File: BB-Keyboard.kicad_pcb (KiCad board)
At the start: 2 copper layers, 41 parts, among them P1 CONN_01X04, SW1 SW_Q, SW10 SW_X, SW11 SW_0, SW12 SW_R, SW13 SW_F, SW14 SW_C, SW15 SW_T, SW16 SW_G, SW17 SW_V, SW18 SW_SPC, SW19 SW_Y, SW2 SW_A, SW20 SW_H, SW21 SW_B, SW22 SW_U, SW23 SW_J, SW24 SW_N, SW25 SW_I, SW26 SW_K, SW27 SW_M, SW28 SW_SYM, SW29 SW_O, SW3 SW_ALT, SW30 SW_L, SW31 SW_$, SW32 SW_RSHIFT, SW33 SW_P, SW34 SW_BK, SW35 SW_ENT, SW4 SW_W, SW5 SW_S, SW6 SW_Z, SW7 SW_LSHIFT, SW8 SW_E, SW9 SW_D, U1 TCA8418

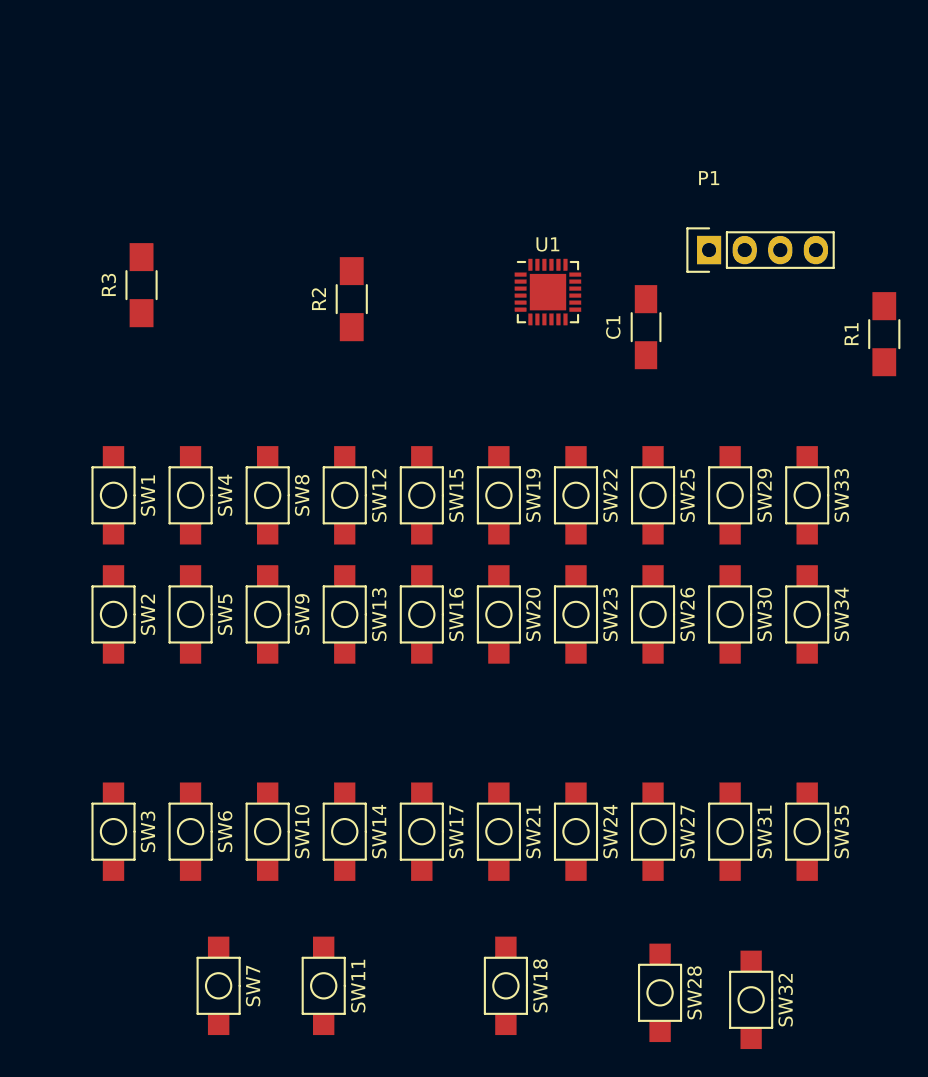
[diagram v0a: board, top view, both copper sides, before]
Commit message: Aligned everything, but the alignment isn't right at all. Needs to be wider.
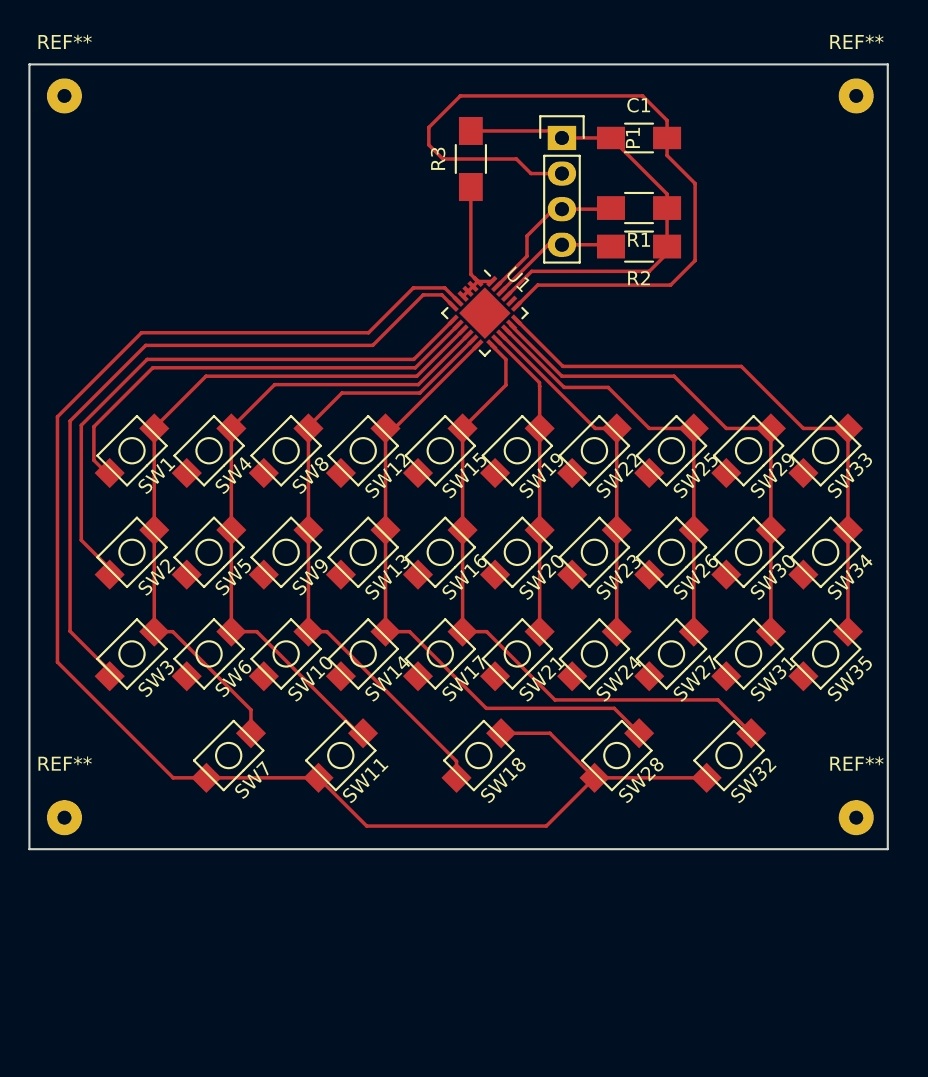
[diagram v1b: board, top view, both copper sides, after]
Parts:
- added REF**: SolderWirePad_single_1mmDrill, Wire_Pads:SolderWirePad_single_1mmDrill, F.Cu at (173.5, 55.5)
- added REF**: SolderWirePad_single_1mmDrill, Wire_Pads:SolderWirePad_single_1mmDrill, F.Cu at (173.5, 107.0)
- added REF**: SolderWirePad_single_1mmDrill, Wire_Pads:SolderWirePad_single_1mmDrill, F.Cu at (117.0, 107.0)
- added REF**: SolderWirePad_single_1mmDrill, Wire_Pads:SolderWirePad_single_1mmDrill, F.Cu at (117.0, 55.5)
- moved R3 25.2 mm to (146.0, 60.0)
- moved R2 20.8 mm to (158.0, 66.2), turned to 180 degrees
- moved R1 19.7 mm to (158.0, 63.5), turned to 180 degrees
- moved SW32 14.5 mm to (167.6, 105.8), turned to 45 degrees
- moved SW28 14.4 mm to (159.6, 105.8), turned to 45 degrees
- moved SW18 13.6 mm to (149.8, 105.8), turned to 45 degrees
- moved C1 13.5 mm to (158.0, 58.5), turned to 0 degrees
- moved SW7 13.3 mm to (131.9, 105.8), turned to 45 degrees
- moved SW11 13.3 mm to (139.9, 105.8), turned to 45 degrees
- moved P1 13.2 mm to (152.5, 58.5), turned to 270 degrees
- moved SW10 9.50 mm to (136.0, 98.5), turned to 45 degrees
- moved SW14 9.50 mm to (141.5, 98.5), turned to 45 degrees
- moved SW17 9.50 mm to (147.0, 98.5), turned to 45 degrees
- moved SW21 9.50 mm to (152.5, 98.5), turned to 45 degrees
- moved SW24 9.50 mm to (158.0, 98.5), turned to 45 degrees
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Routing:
- net /ROW3: track 0.00 -> 110.9 mm
- net GND: track 0.00 -> 55.2 mm
- net /ROW2: track 0.00 -> 50.8 mm
- net /COL0: track 0.00 -> 50.3 mm
- net /COL1: track 0.00 -> 46.6 mm
- net /COL4: track 0.00 -> 45.8 mm
- net /COL3: track 0.00 -> 44.7 mm
- net /COL2: track 0.00 -> 44.5 mm
- net /COL9: track 0.00 -> 41.3 mm
- net /ROW1: track 0.00 -> 41.1 mm
- net /COL8: track 0.00 -> 36.1 mm
- net /ROW0: track 0.00 -> 32.9 mm
- net +3V3: track 0.00 -> 32.8 mm
- net /COL7: track 0.00 -> 30.8 mm
- net /COL6: track 0.00 -> 25.5 mm
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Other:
- board outline added: 61.2 x 56 mm
